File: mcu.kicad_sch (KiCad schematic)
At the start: 38 parts, among them J2 RJ45_Shielded, J3 RJ45_Shielded, J4 Micro_SD_Card_Det1, J6 Conn_01x03_Pin, SW1 SW_Push, SW2 SW_Push, SW3 SW_Push, SW4 SW_Push, U1 nRF54L15-QFXX, U9 TPD6F003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

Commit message: improve design a lot
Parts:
- removed J3: RJ45_Shielded, Connector_RJ:RJ45_Amphenol_54602-x08_Horizontal, symbol Connector:RJ45_Shielded
- added J7: RFShield_TwoPieces, RF_Shielding:Laird_Technologies_BMI-S-103_26.21x26.21mm, symbol Device:RFShield_TwoPieces
- C19, C20, C21: footprint (none) -> Capacitor_SMD:C_0201_0603Metric
- J2: footprint Connector_RJ:RJ45_Amphenol_54602-x08_Horizontal -> Connector_RJ:RJ45_Amphenol_RJHSE538X
- L3, L4, L5: footprint (none) -> Inductor_SMD:L_0201_0603Metric
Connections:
- net 1.8V: now also J2.2; no longer J2.3
- net DETECT1: now also J2.3; no longer J2.6
- net DETECT2: now also J2.4
- net GND: now also J2.1, J7.1 (Shield); no longer J2.2, J2.7
- net SENSE1B: now also J2.6; no longer J2.4
- net SENSE2A: now also J2.7
- net SENSE2B: now also J2.8
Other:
- moved on the sheet: J2

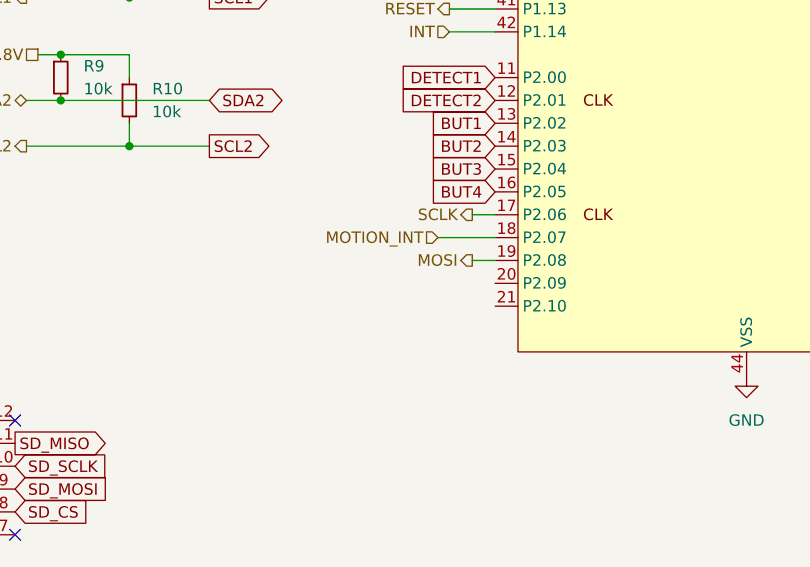
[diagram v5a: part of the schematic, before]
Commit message: finish oled driver circuit
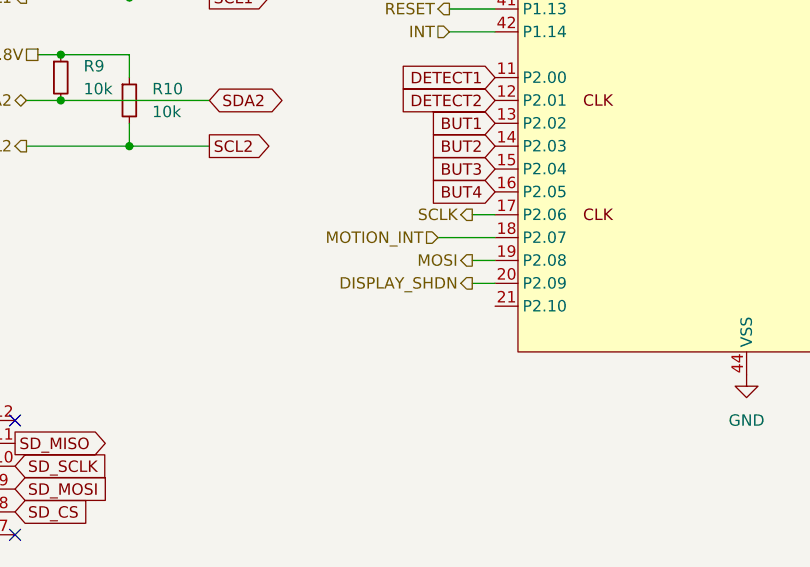
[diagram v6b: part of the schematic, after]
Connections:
- net DISPLAY_SHDN: now reaches U1.20 (P2.09)
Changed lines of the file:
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@@
+	(wire
+		(pts
+			(xy 173.99 148.59) (xy 176.53 148.59)
+		)
+		(stroke
+			(width 0)
+			(type default)
+		)
+	)
 	(wire
 		(pts
@@
 		(effects
 			(font
+				(size 1.27 1.27)
+			)
+			(justify right)
+		)
+	)
+	(hierarchical_label "DISPLAY_SHDN"
+		(shape output)
+		(at 173.99 148.59 180)
+		(effects
+			(font

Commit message: route SD card traces and antenna traces semi-properly
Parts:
- Y1: footprint (none) -> Library:CRYSTAL-SMD_L3.2-W1.5-1
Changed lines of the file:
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@@
 			)
 		)
-		(property "Footprint" ""
+		(property "Footprint" "Library:CRYSTAL-SMD_L3.2-W1.5-1"
 			(at 160.02 52.07 0)
 			(effects

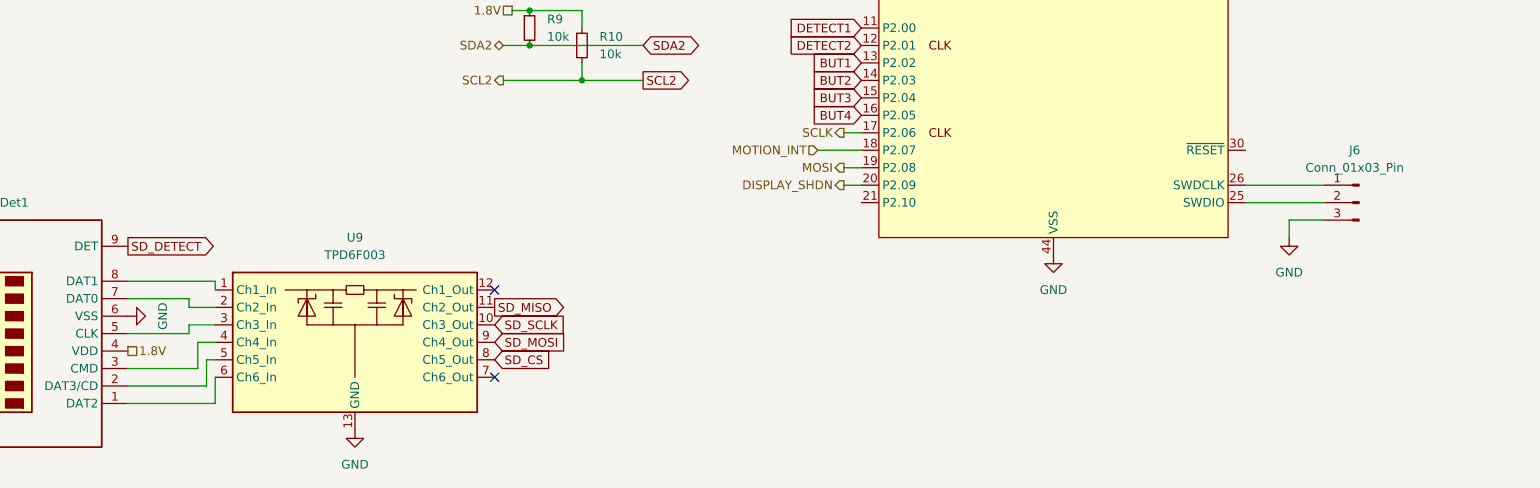
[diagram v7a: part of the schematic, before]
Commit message: route SWD lines
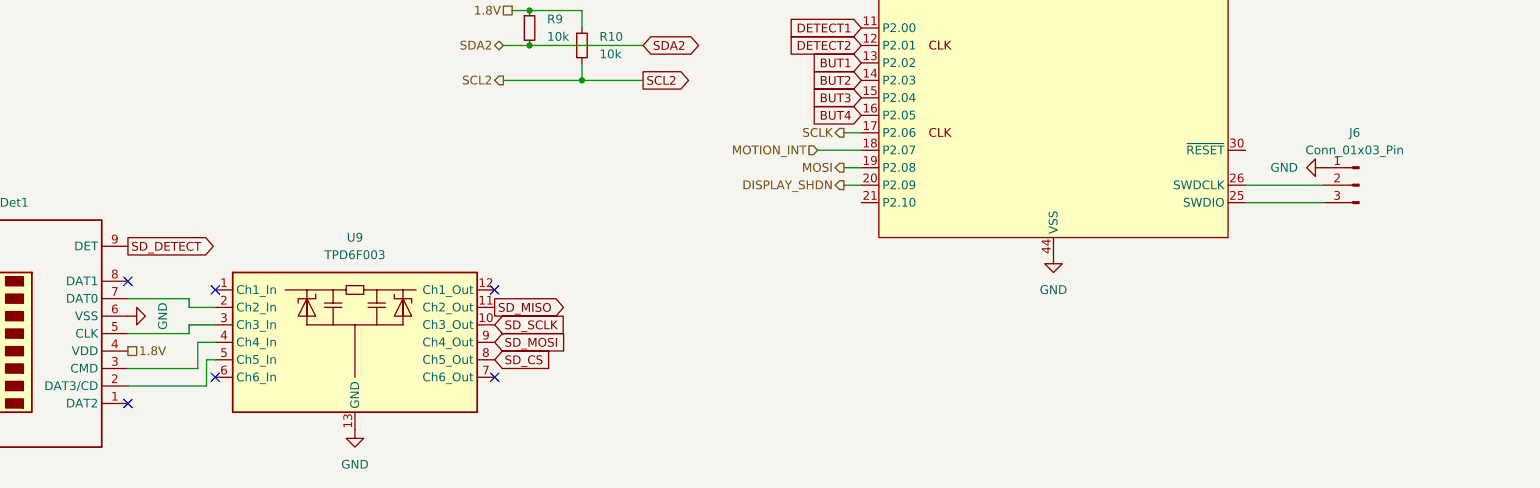
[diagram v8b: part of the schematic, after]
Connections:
- net GND: now also J6.1 (Pin_1); no longer J6.3 (Pin_3)
- net at U9.1 (Ch1_In): no longer J4.8 (DAT1)
- net at U9.6 (Ch6_In): no longer J4.1 (DAT2)
- net at U1.25 (SWDIO): now also J6.3 (Pin_3); no longer J6.2 (Pin_2)
- net at U1.26 (SWDCLK): now also J6.2 (Pin_2); no longer J6.1 (Pin_1)
- no-connect marks 2 -> 6
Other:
- moved on the sheet: J6
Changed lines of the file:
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@@
 	)
 	(no_connect
+		(at 82.55 176.53)
+	)
+	(no_connect
+		(at 69.85 162.56)
+	)
+	(no_connect
+		(at 82.55 163.83)
+	)
+	(no_connect
 		(at 123.19 176.53)
 	)
+	(no_connect
+		(at 69.85 180.34)
+	)
 	(wire
 		(pts
@@
 	(wire
 		(pts
-			(xy 82.55 176.53) (xy 82.55 180.34)
-		)
-		(stroke
-			(width 0)
-			(type default)
-		)
-	)
-	(wire
-		(pts
 			(xy 170.18 33.02) (xy 181.61 33.02)
 		)
@@
 	(wire
 		(pts
-			(xy 232.41 148.59) (xy 243.84 148.59)
-		)
-		(stroke
-			(width 0)
-			(type default)
-		)
-	)
-	(wire
-		(pts
 			(xy 81.28 177.8) (xy 69.85 177.8)
 		)
@@
 	(wire
 		(pts
-			(xy 128.27 111.76) (xy 144.78 111.76)
+			(xy 232.41 151.13) (xy 243.84 151.13)
 		)
 		(stroke
@@
 	(wire
 		(pts
-			(xy 232.41 59.69) (xy 234.95 59.69)
+			(xy 128.27 111.76) (xy 144.78 111.76)
 		)
 		(stroke
@@
 	(wire
 		(pts
-			(xy 144.78 30.48) (xy 144.78 33.02)
+			(xy 232.41 59.69) (xy 234.95 59.69)
 		)
 		(stroke
@@
 	(wire
 		(pts
-			(xy 247.65 100.33) (xy 255.27 100.33)
+			(xy 144.78 30.48) (xy 144.78 33.02)
 		)
 		(stroke
@@
 	(wire
 		(pts
-			(xy 234.95 54.61) (xy 232.41 54.61)
+			(xy 247.65 100.33) (xy 255.27 100.33)
 		)
 		(stroke
@@
 	(wire
 		(pts
-			(xy 181.61 38.1) (xy 194.31 38.1)
+			(xy 234.95 54.61) (xy 232.41 54.61)
 		)
 		(stroke
@@
 	(wire
 		(pts
-			(xy 135.89 125.73) (xy 135.89 123.19)
+			(xy 181.61 38.1) (xy 194.31 38.1)
 		)
 		(stroke
@@
 	(wire
 		(pts
-			(xy 82.55 163.83) (xy 82.55 162.56)
+			(xy 135.89 125.73) (xy 135.89 123.19)
 		)
 		(stroke
@@
 	(wire
 		(pts
-			(xy 243.84 153.67) (xy 238.76 153.67)
-		)
-		(stroke
-			(width 0)
-			(type default)
-		)
-	)
-	(wire
-		(pts
 			(xy 157.48 33.02) (xy 170.18 33.02)
 		)
@@
 	(wire
 		(pts
-			(xy 82.55 162.56) (xy 69.85 162.56)
-		)
-		(stroke
-			(width 0)
-			(type default)
-		)
-	)
-	(wire
-		(pts
-			(xy 238.76 153.67) (xy 238.76 156.21)
-		)
-		(stroke
-			(width 0)
-			(type default)
-		)
-	)
-	(wire
-		(pts
 			(xy 243.84 49.53) (xy 262.89 49.53)
 		)
@@
 	(wire
 		(pts
-			(xy 82.55 180.34) (xy 69.85 180.34)
-		)
-		(stroke
-			(width 0)
-			(type default)
-		)
-	)
-	(wire
-		(pts
 			(xy 252.73 52.07) (xy 262.89 52.07)
 		)
@@
 	(wire
 		(pts
-			(xy 232.41 151.13) (xy 243.84 151.13)
+			(xy 124.46 111.76) (xy 128.27 111.76)
 		)
 		(stroke
@@
 	(wire
 		(pts
-			(xy 124.46 111.76) (xy 128.27 111.76)
+			(xy 78.74 170.18) (xy 78.74 168.91)
 		)
 		(stroke
@@
 	(wire
 		(pts
-			(xy 78.74 170.18) (xy 78.74 168.91)
+			(xy 232.41 148.59) (xy 243.84 148.59)
 		)
 		(stroke
@@
 	(symbol
 		(lib_id "Connector:Conn_01x03_Pin")
-		(at 248.92 151.13 0)
+		(at 248.92 148.59 0)
 		(mirror y)
 		(unit 1)
@@
 		(dnp no)
 		(property "Reference" "J6"
-			(at 248.285 143.51 0)
+			(at 248.285 140.97 0)
 			(effects
 				(font
@@
 		)
 		(property "Value" "Conn_01x03_Pin"
-			(at 248.285 146.05 0)
+			(at 248.285 143.51 0)
 			(effects
 				(font
@@
 		)
 		(property "Footprint" "Connector_PinHeader_1.27mm:PinHeader_1x03_P1.27mm_Vertical"
-			(at 248.92 151.13 0)
+			(at 248.92 148.59 0)
 			(effects
 				(font
@@
 		)
 		(property "Datasheet" "~"
-			(at 248.92 151.13 0)
+			(at 248.92 148.59 0)
 			(effects
 				(font
@@
 		)
 		(property "Description" "Generic connector, single row, 01x03, script generated"
-			(at 248.92 151.13 0)
+			(at 248.92 148.59 0)
 			(effects
 				(font
@@
 	(symbol
 		(lib_id "power:GND")
-		(at 238.76 156.21 0)
+		(at 243.84 146.05 270)
 		(unit 1)
 		(exclude_from_sim no)
@@
 		(fields_autoplaced yes)
 		(property "Reference" "#PWR051"
-			(at 238.76 162.56 0)
+			(at 237.49 146.05 0)
 			(effects
 				(font
@@
 		)
 		(property "Value" "GND"
-			(at 238.76 161.29 0)
+			(at 240.03 146.0499 90)
 			(effects
 				(font
 					(size 1.27 1.27)
 				)
+				(justify right)
 			)
 		)
 		(property "Footprint" ""
-			(at 238.76 156.21 0)
+			(at 243.84 146.05 0)
 			(effects
 				(font
@@
 		)
 		(property "Datasheet" ""
-			(at 238.76 156.21 0)
+			(at 243.84 146.05 0)
 			(effects
 				(font
@@
 		)
 		(property "Description" "Power symbol creates a global label with name \"GND\" , ground"
-			(at 238.76 156.21 0)
+			(at 243.84 146.05 0)
 			(effects
 				(font
